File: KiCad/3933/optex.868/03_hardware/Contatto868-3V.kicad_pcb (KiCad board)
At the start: 2 copper layers, 96.8 x 15.5 mm, 54 parts, among them CN3 STRIP Prog., P1 SERIAL CONNECTOR, P2 JBAT, P3 TAMPER CONNECTOR, Q1 Q_NMOS_DGS, U1 SI4432B, U2 MSP430G2433IRHN32, U5 UPG2214TB

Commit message: Kicad and firmware updates
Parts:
- U1: footprint Housings_DFN_QFN:QFN-20-1EP_4x4mm_Pitch0.5mm -> saet:QFN-20-1EP_4x4mm_Pitch0.5mm_with_back_holes
- U2: footprint Housings_DFN_QFN:QFN-32-1EP_5x5mm_Pitch0.5mm -> saet:QFN-32-1EP_5x5mm_Pitch0.5mm_with_back_holes
- moved C17 1.51 mm to (125.8, 113.3)
- moved Q1 1.00 mm to (160.4, 109.6), turned to 180 degrees
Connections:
- Q1 pad 1: /Yellow -> Net-(Q1-Pad1)
- Q1 pad 2: Net-(Q1-Pad2) -> /TX
- Q1 pad 3: /TX -> /Yellow
- QZ1 pad 2: Net-(QZ1-Pad2) -> (no net)
- QZ1 pad 3: (no net) -> Net-(QZ1-Pad2)
- R2 pad 1: Net-(Q1-Pad2) -> Net-(Q1-Pad1)
- U1 pad 21: (no net) -> GND
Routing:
- net GND: track 197.5 -> 267.9 mm, vias 15 -> 46
- net Net-(QZ1-Pad2): track 4.14 -> 7.46 mm
- net Net-(Q1-Pad2): track 2.33 -> 0.00 mm
- net Net-(Q1-Pad1): track 0.00 -> 1.91 mm
- net /TX: track 2.31 -> 4.02 mm
- net (no net): vias 48 -> 0

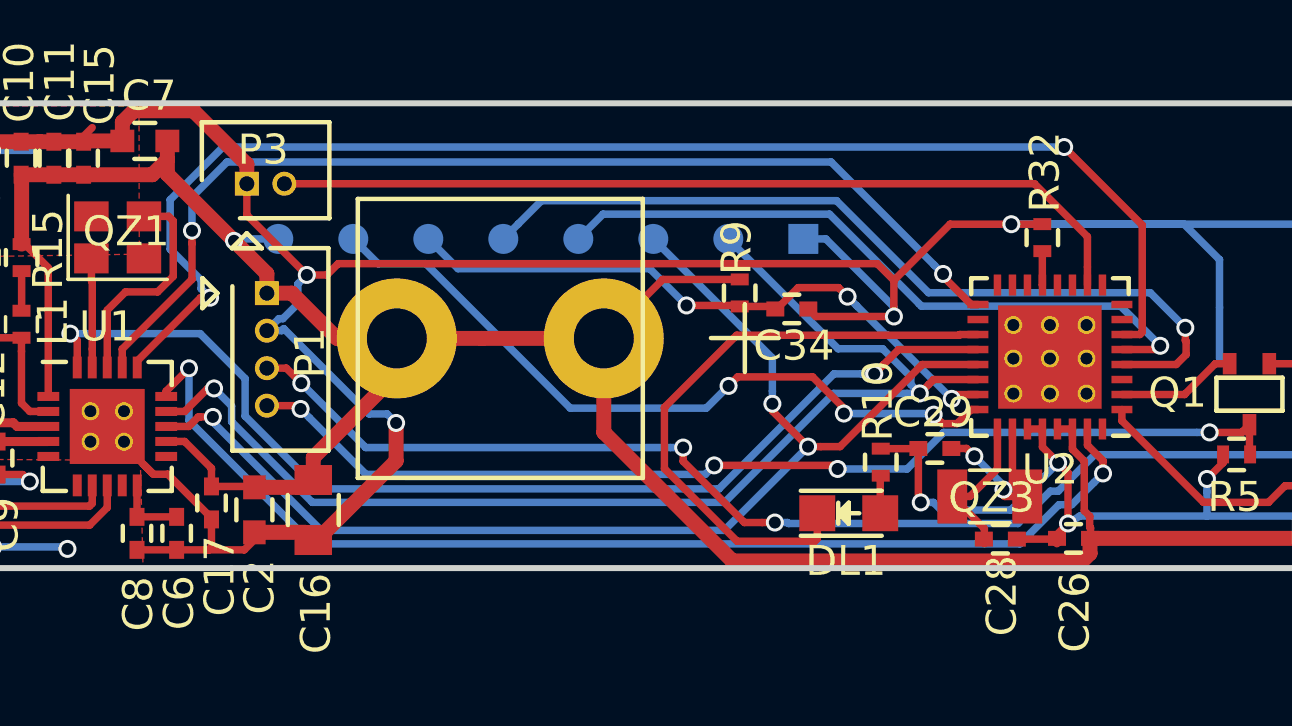
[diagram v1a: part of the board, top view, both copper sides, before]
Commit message: Aggiornamenti su modulo SPI (sw->hw) e vari sui circuiti
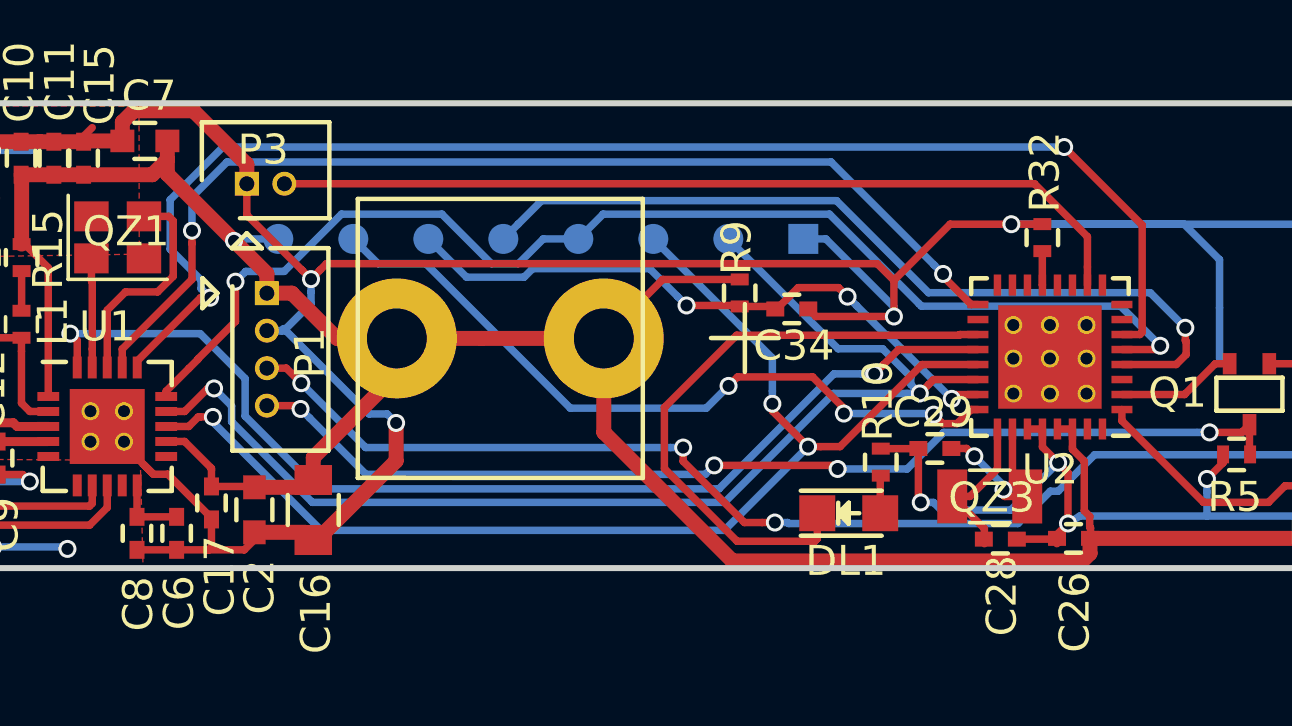
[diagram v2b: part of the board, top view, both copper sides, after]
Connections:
- CN3 pad 4: Net-(CN3-Pad4) -> CLK
- U2 pad 31: CLK -> Net-(U2-Pad31)
- U2 pad 5: Net-(CN3-Pad4) -> CLK
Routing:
- net Net-(CN3-Pad4): track 22.9 -> 0.00 mm, vias 1 -> 0
- net CLK: track 37.8 -> 41.1 mm
